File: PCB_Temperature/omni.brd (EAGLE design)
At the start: 70 x 53.6 mm, 12 parts

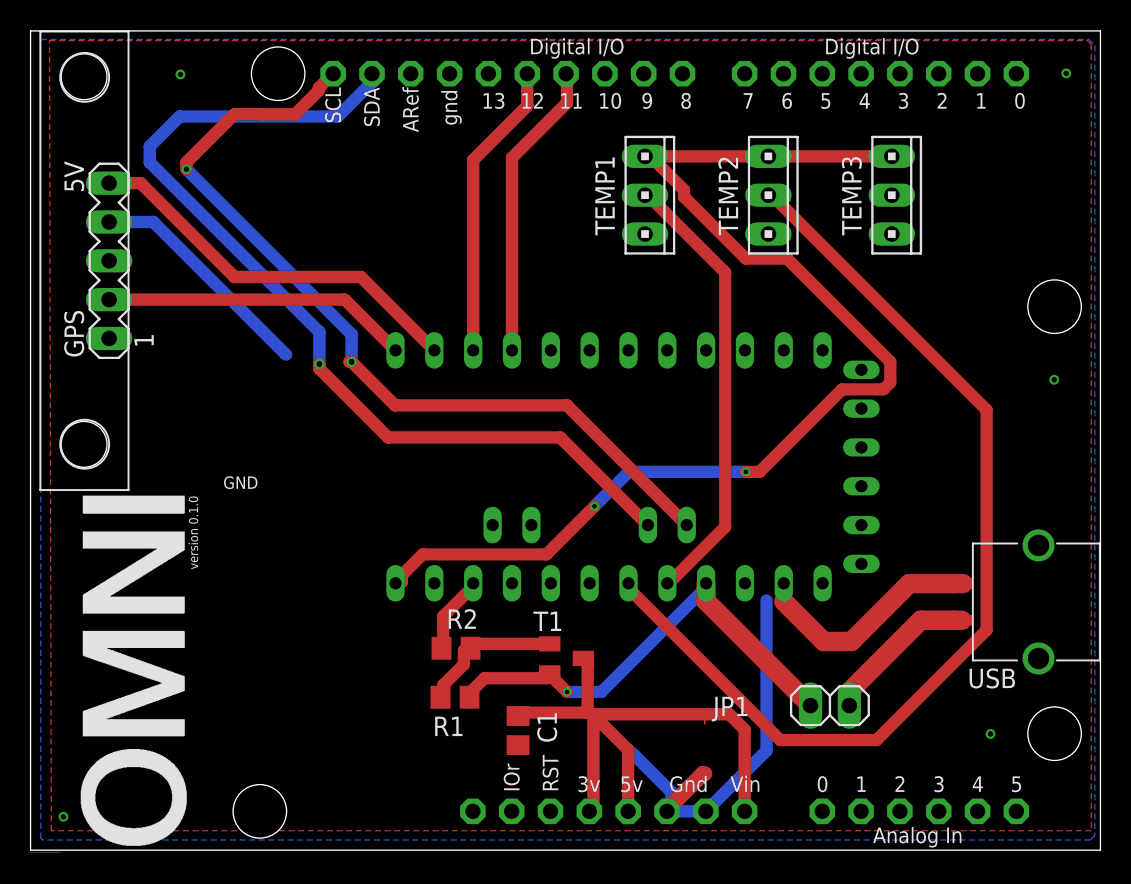
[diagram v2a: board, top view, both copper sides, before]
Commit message: Fix the missing connection with Temp3
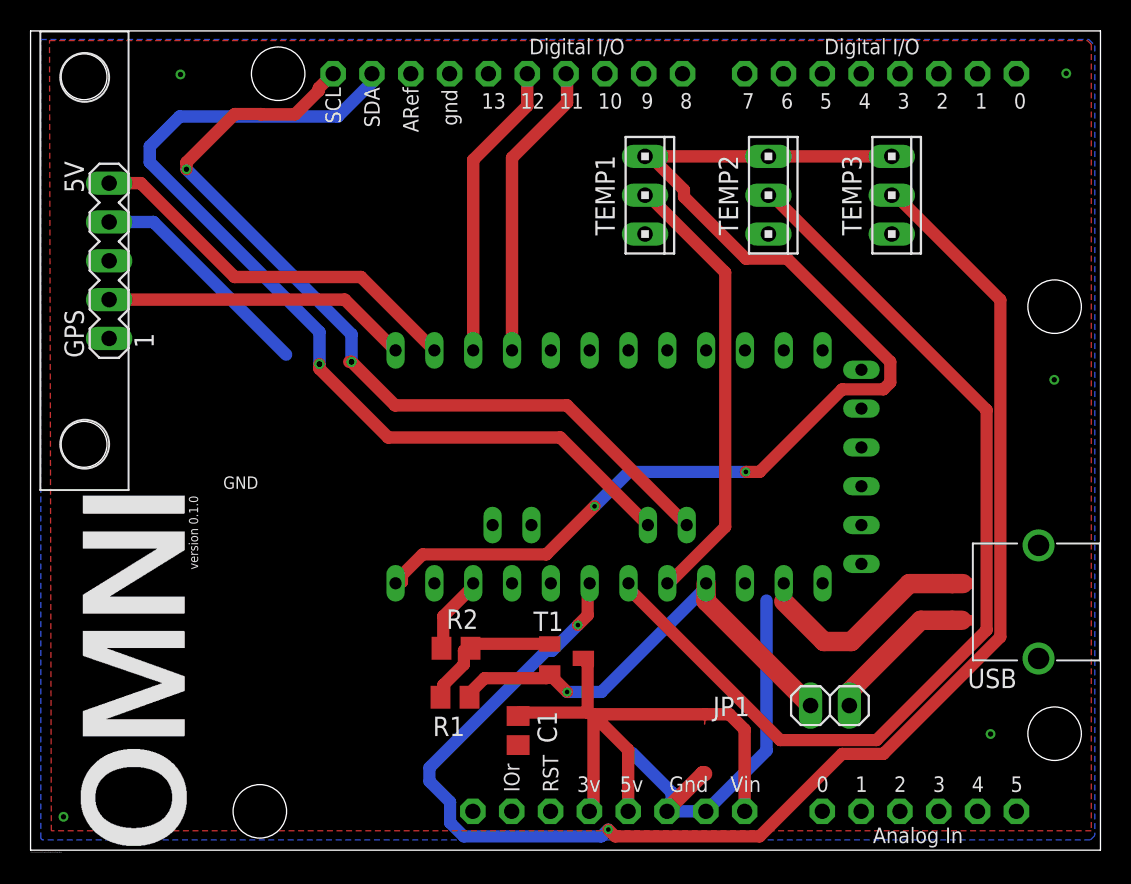
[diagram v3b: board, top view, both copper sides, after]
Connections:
- new net S$4: TEMP3.2, U$1.A2
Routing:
- net S$4: track 0.00 -> 94.9 mm, vias 0 -> 2
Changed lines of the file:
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@@
 <wire x1="28.8" y1="17.1" x2="28.96" y2="17.46" width="0.8" layer="1"/>
+</signal>
+<signal name="S$4">
+<contactref element="U$1" pad="A2"/>
+<contactref element="TEMP3" pad="2"/>
+<wire x1="36.45" y1="15.3660375" x2="36.45" y2="17.1" width="0.8" layer="1"/>
+<wire x1="35.8141625" y1="14.7302" x2="36.45" y2="15.3660375" width="0.8" layer="1"/>
+<wire x1="34.1339625" y1="13.05" x2="35.8141625" y2="14.7302" width="0.8" layer="16"/>
+<wire x1="33.75" y1="13.05" x2="34.1339625" y2="13.05" width="0.8" layer="16"/>
+<wire x1="26.1" y1="5.4" x2="33.75" y2="13.05" width="0.8" layer="16"/>
+<wire x1="26.1" y1="4.5" x2="26.1" y2="5.4" width="0.8" layer="16"/>
+<wire x1="27.45" y1="3.15" x2="26.1" y2="4.5" width="0.8" layer="16"/>
+<wire x1="27.45" y1="1.8" x2="27.45" y2="3.15" width="0.8" layer="16"/>
+<wire x1="28.35" y1="0.9" x2="27.45" y2="1.8" width="0.8" layer="16"/>
+<wire x1="37.35" y1="0.9" x2="28.35" y2="0.9" width="0.8" layer="16"/>
+<wire x1="37.8" y1="1.35" x2="37.35" y2="0.9" width="0.8" layer="16"/>
+<wire x1="38.25" y1="0.9" x2="37.8" y2="1.35" width="0.8" layer="1"/>
+<wire x1="47.7" y1="0.9" x2="38.25" y2="0.9" width="0.8" layer="1"/>
+<wire x1="53.1" y1="6.3" x2="47.7" y2="0.9" width="0.8" layer="1"/>
+<wire x1="55.8" y1="6.3" x2="53.1" y2="6.3" width="0.8" layer="1"/>
+<wire x1="63.45" y1="13.95" x2="55.8" y2="6.3" width="0.8" layer="1"/>
+<wire x1="63.45" y1="36" x2="63.45" y2="13.95" width="0.8" layer="1"/>
+<wire x1="56.7" y1="42.75" x2="63.45" y2="36" width="0.8" layer="1"/>
+<wire x1="36.45" y1="17.1" x2="36.58" y2="17.46" width="0.8" layer="1"/>
+<wire x1="56.7" y1="42.75" x2="56.348625" y2="42.851703125" width="0.8" layer="1"/>
+<via x="35.8141625" y="14.7302" extent="1-16" drill="0.3"/>
+<via x="37.8" y="1.35" extent="1-16" drill="0.3"/>
 </signal>
 </signals>
